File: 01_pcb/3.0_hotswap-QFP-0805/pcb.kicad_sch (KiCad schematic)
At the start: 126 parts, among them J2 AVR-ISP-6_mod, J3 4PIN, J5 Conn_01x08, SW1 SW_PUSH, U1 ATmega32U4-A, U2 PRTR5V0U2X, Y1 16MHz

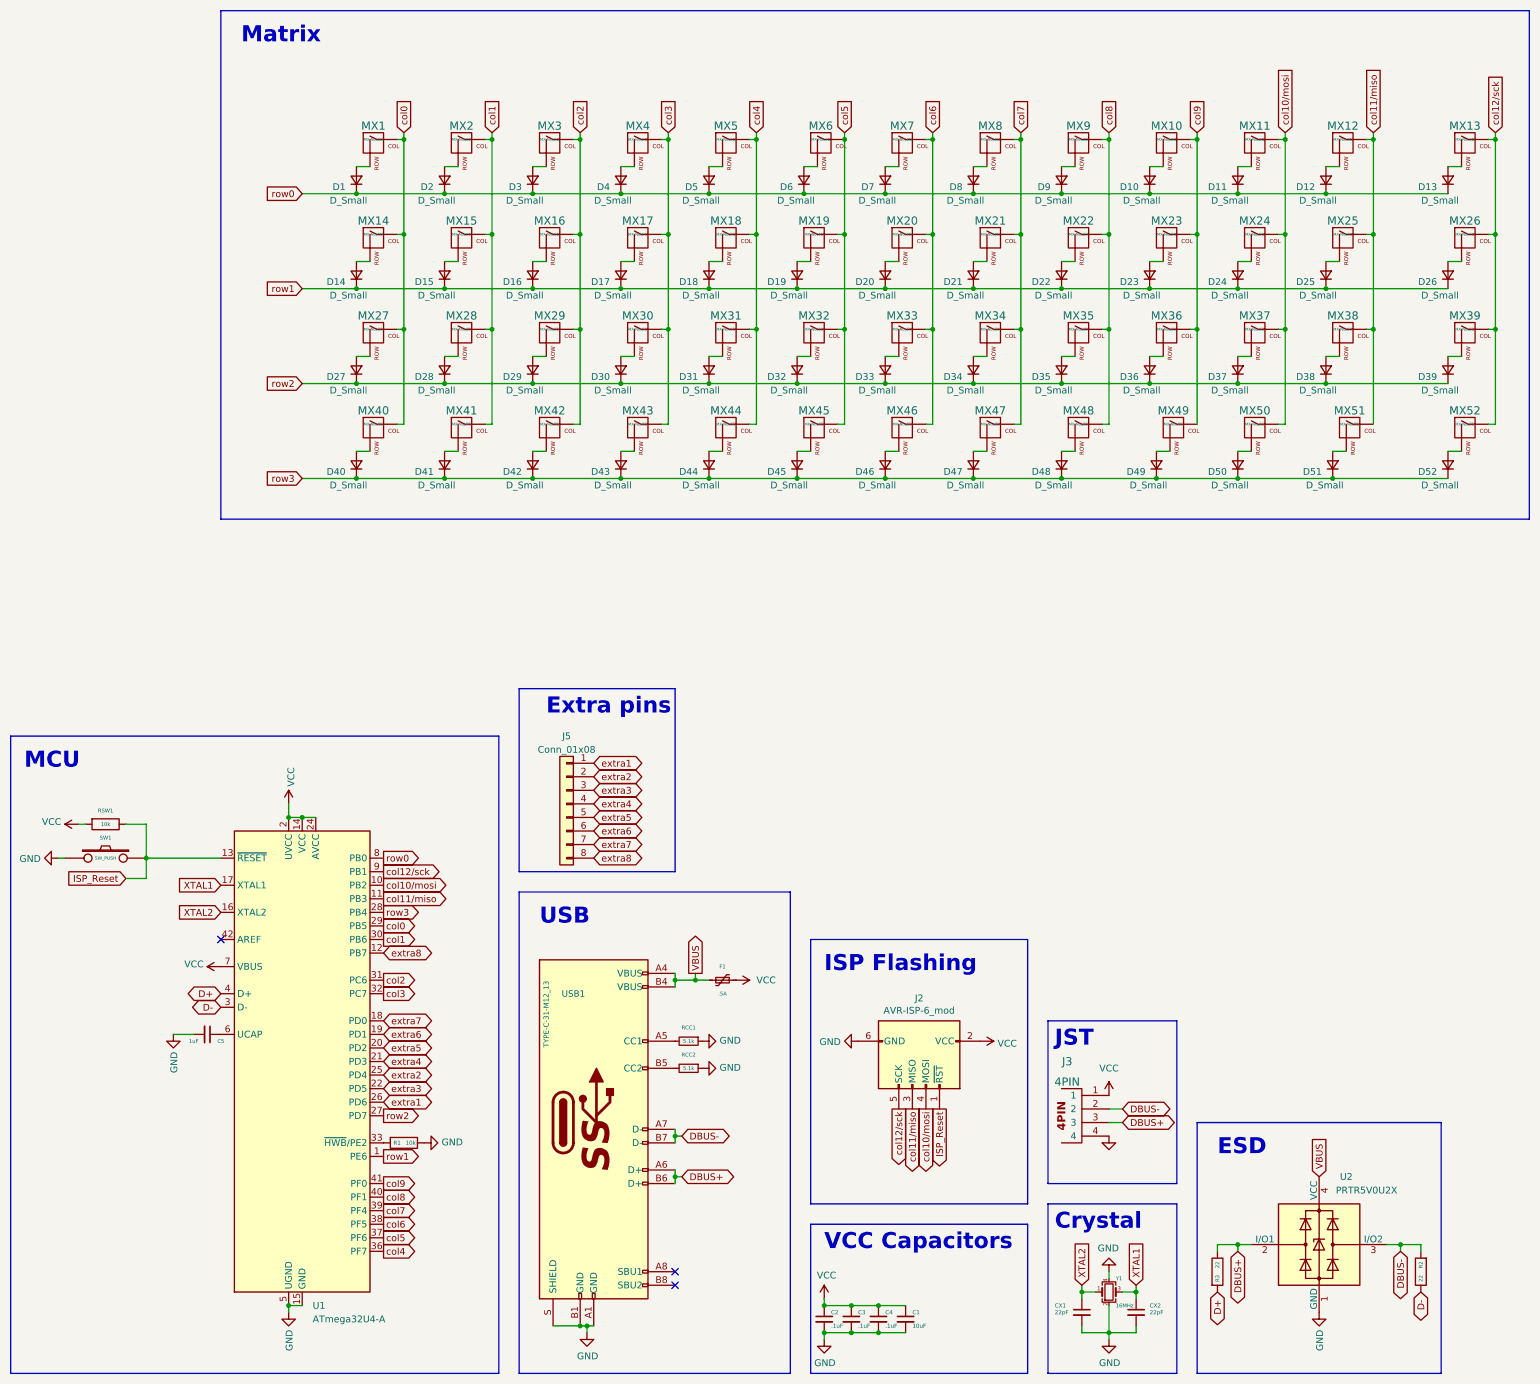
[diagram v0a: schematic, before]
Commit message: remove usb - only daughterboard now
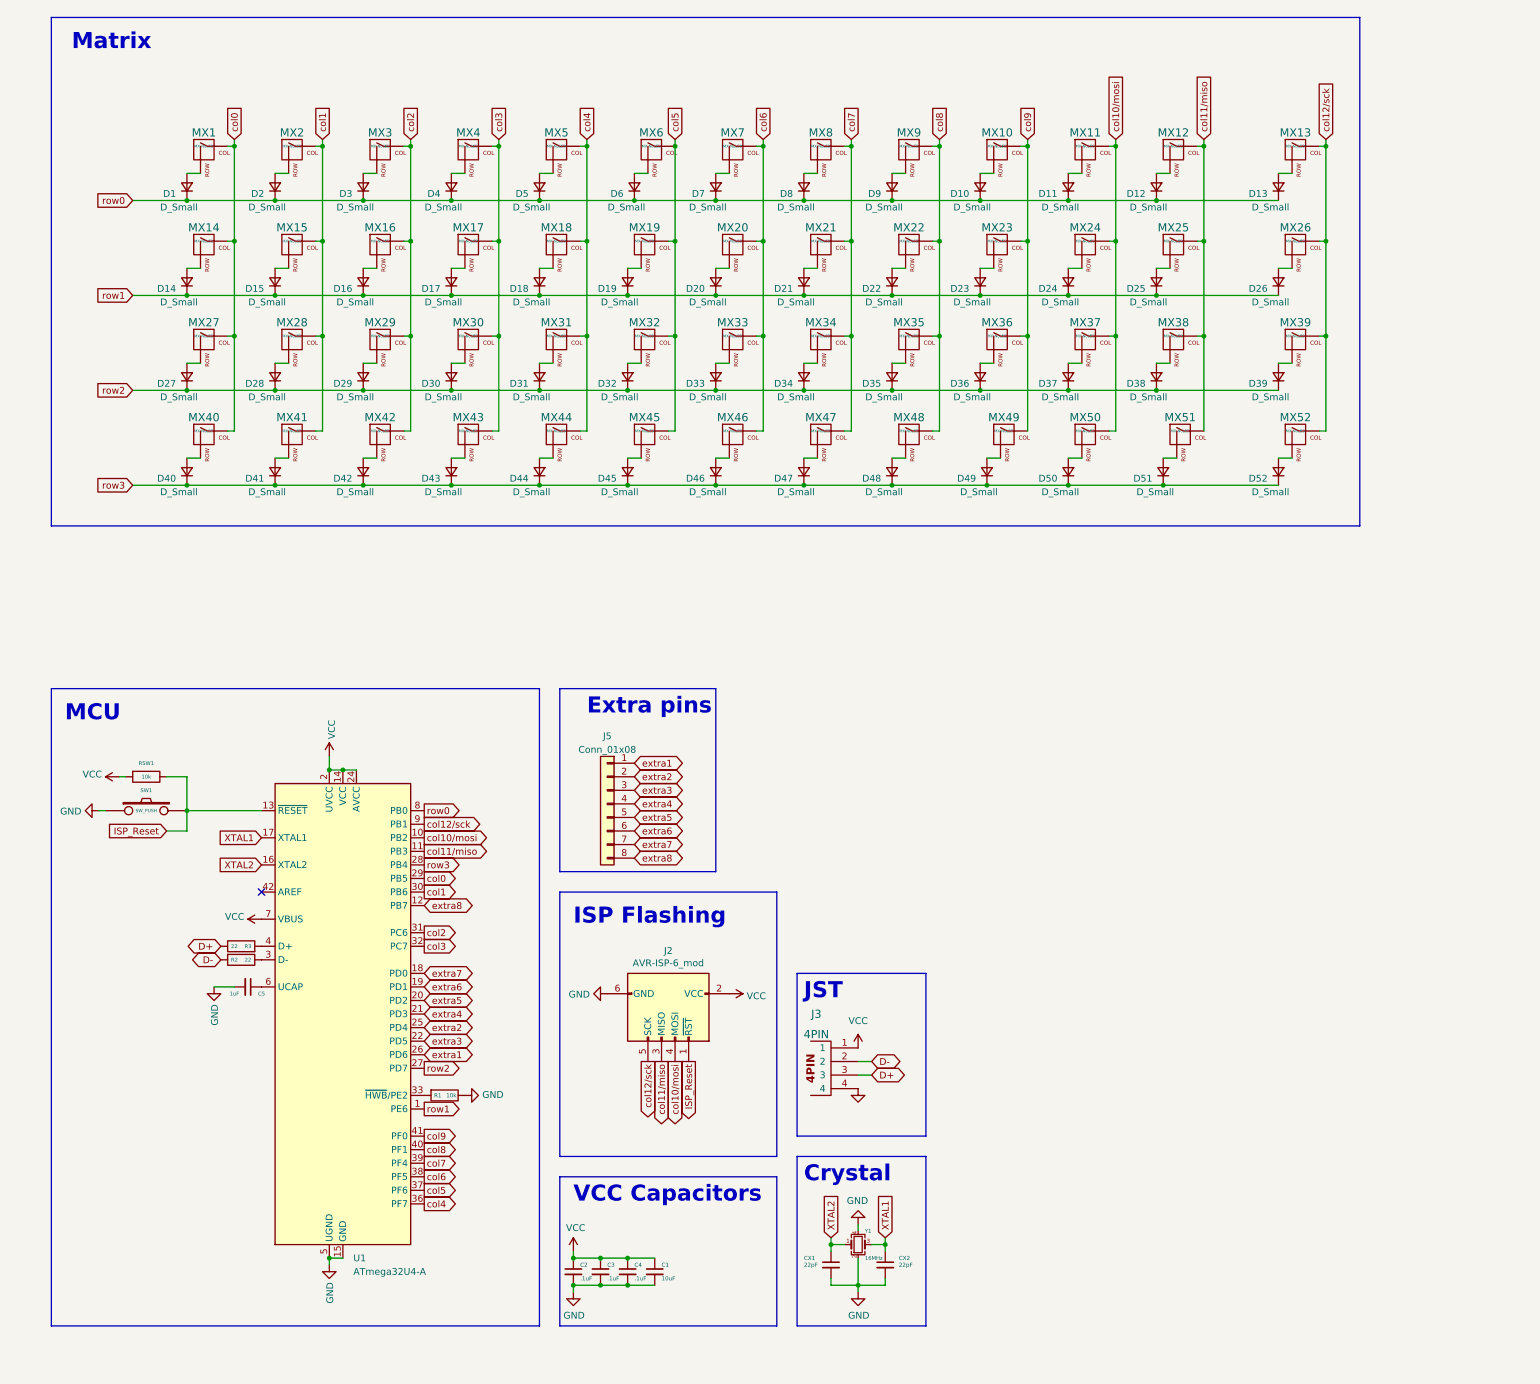
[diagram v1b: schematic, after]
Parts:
- removed F1: .5A, Fuse:Fuse_0805_2012Metric_Pad1.15x1.40mm_HandSolder, symbol Device:Polyfuse_Small
- removed RCC1, RCC2: 5.1k, Resistor_SMD:R_0805_2012Metric, symbol Device:R_Small
- removed U2: PRTR5V0U2X, Package_TO_SOT_SMD:SOT-143, symbol Power_Protection:PRTR5V0U2X
- removed USB1: TYPE-C-31-M12_13, acheron_Connectors:TYPE-C-31-M-12, symbol pcb-rescue:TYPE-C-31-M12_13-acheronSymbols-Ori-rescue-lucy-rescue
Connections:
- net DBUS+ is gone; now on net D+: J3.3, R3.1
- net DBUS- is gone; now on net D-: J3.2, R2.2
- net D+: no longer R3.2, U1.4 (D+)
- net D-: no longer R2.1, U1.3 (D-)
- new net: R3.2, U1.4 (D+)
- new net: R2.1, U1.3 (D-)
- no-connect marks 3 -> 1
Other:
- note removed: "ESD"
- note removed: "USB"
- moved on the sheet: C1, C2, C3, C4, C5, CX1, CX2, D1, D10, D11, D12, D13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
